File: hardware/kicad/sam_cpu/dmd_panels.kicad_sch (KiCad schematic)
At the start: 20 parts, among them J25 J25 HUB75 PANEL A, J26 J26 HUB75 PANEL B, U27 74AHCT245, U28 74AHCT245, U29 74AHCT245, U30 74HC165, U31 74HC595

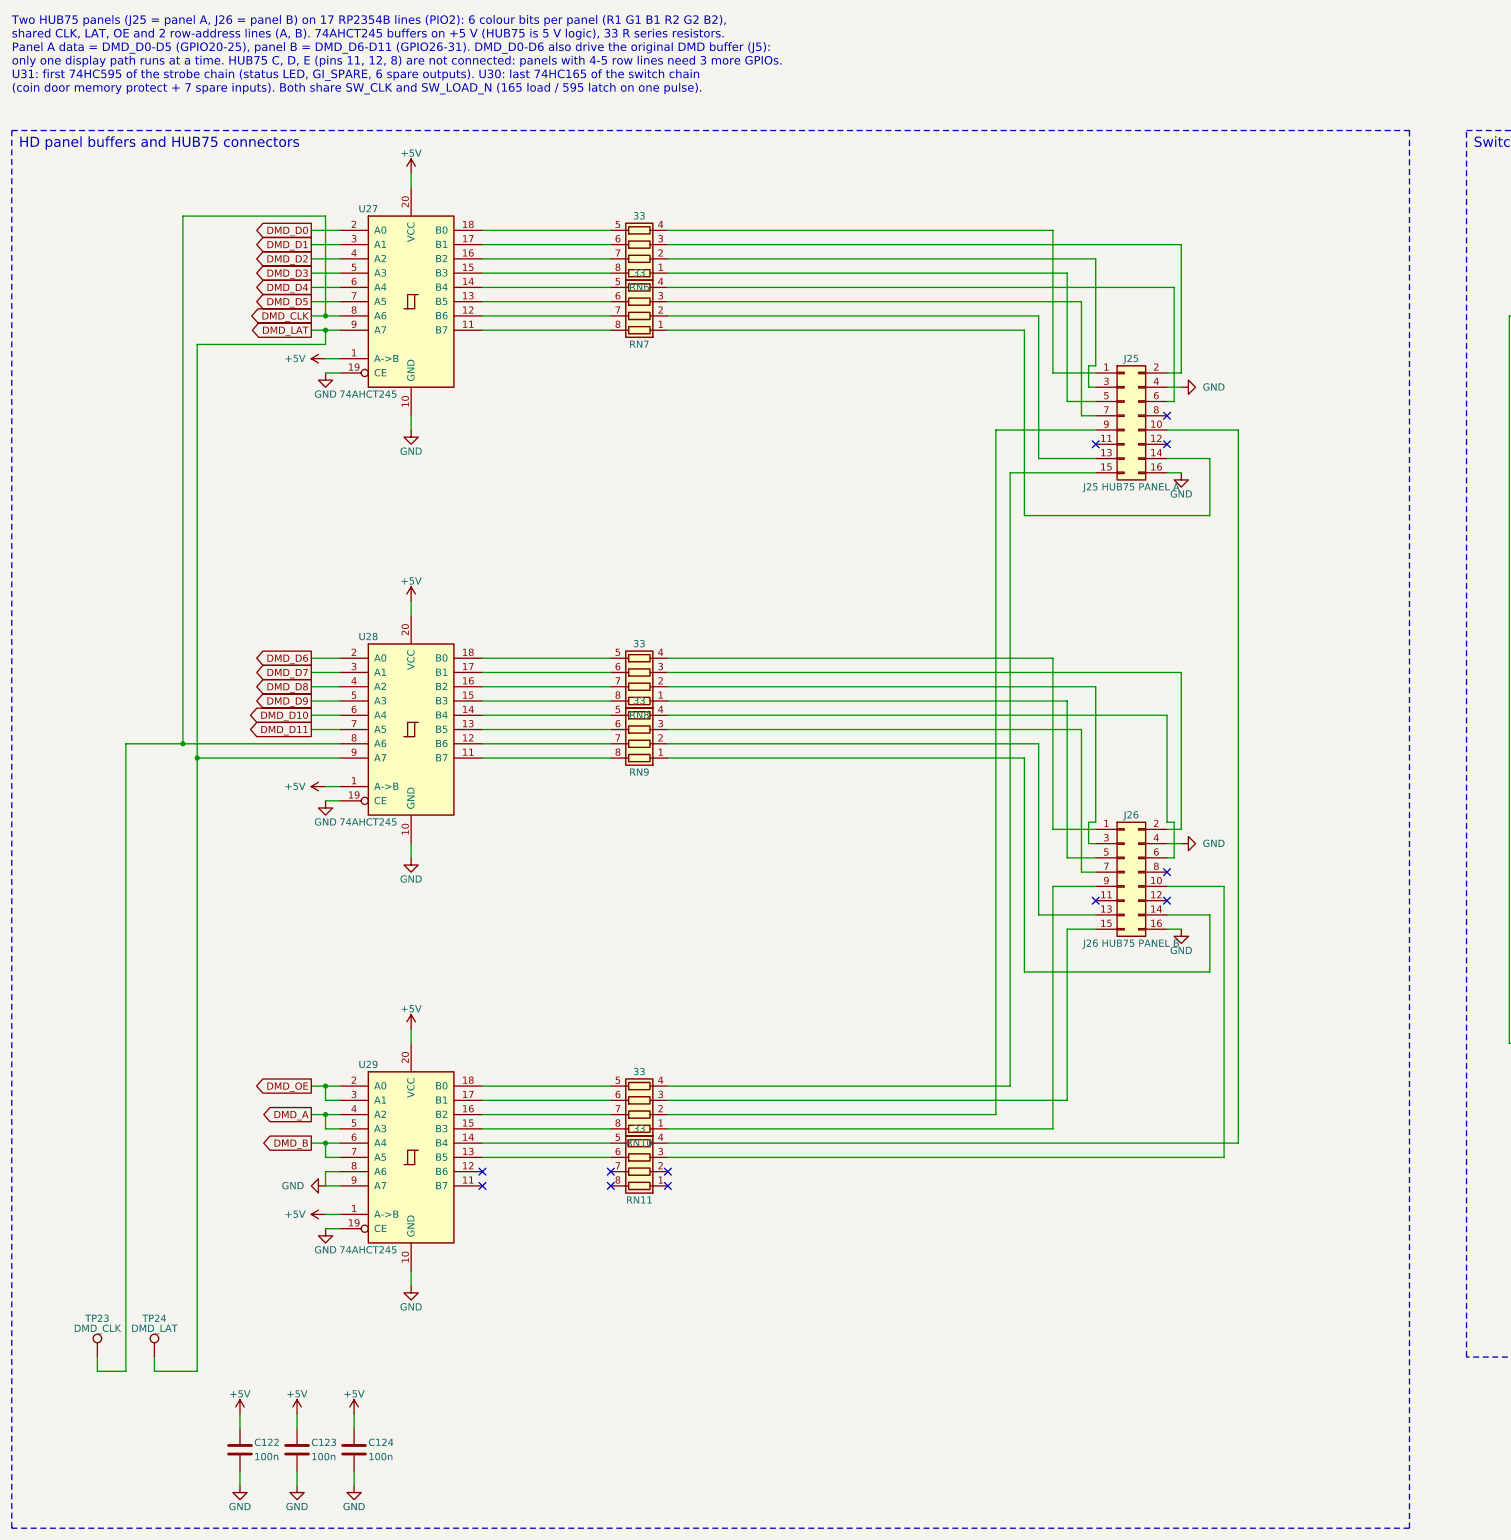
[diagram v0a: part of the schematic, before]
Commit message: Remove both DMD interfaces from the schematic and the board
DMD signals do not survive the long cabinet wires (Vincent, 2026-10-07).
Removed: J5 original DMD driver (U21, RN4, RN5, R176-R182, C95) and the
HD panel bus (J25, J26, U27-U29, RN6-RN11, C122-C124, TP23, TP24), their
tracks and fan-out vias. U30 / U31 stay (switch chain). RP2354B GPIO20-36
are unassigned (no-connect flags). The board goes back to the original
120.65 x 231.76 mm outline. DRC: 20 connections still open (was 35).

Co-Authored-By: Claude Opus 5.5 (1M context) <noreply@anthropic.com>
Claude-Session: https://claude.ai/code/session_01ExuDVoDDDHhVWjb8EwVzYb
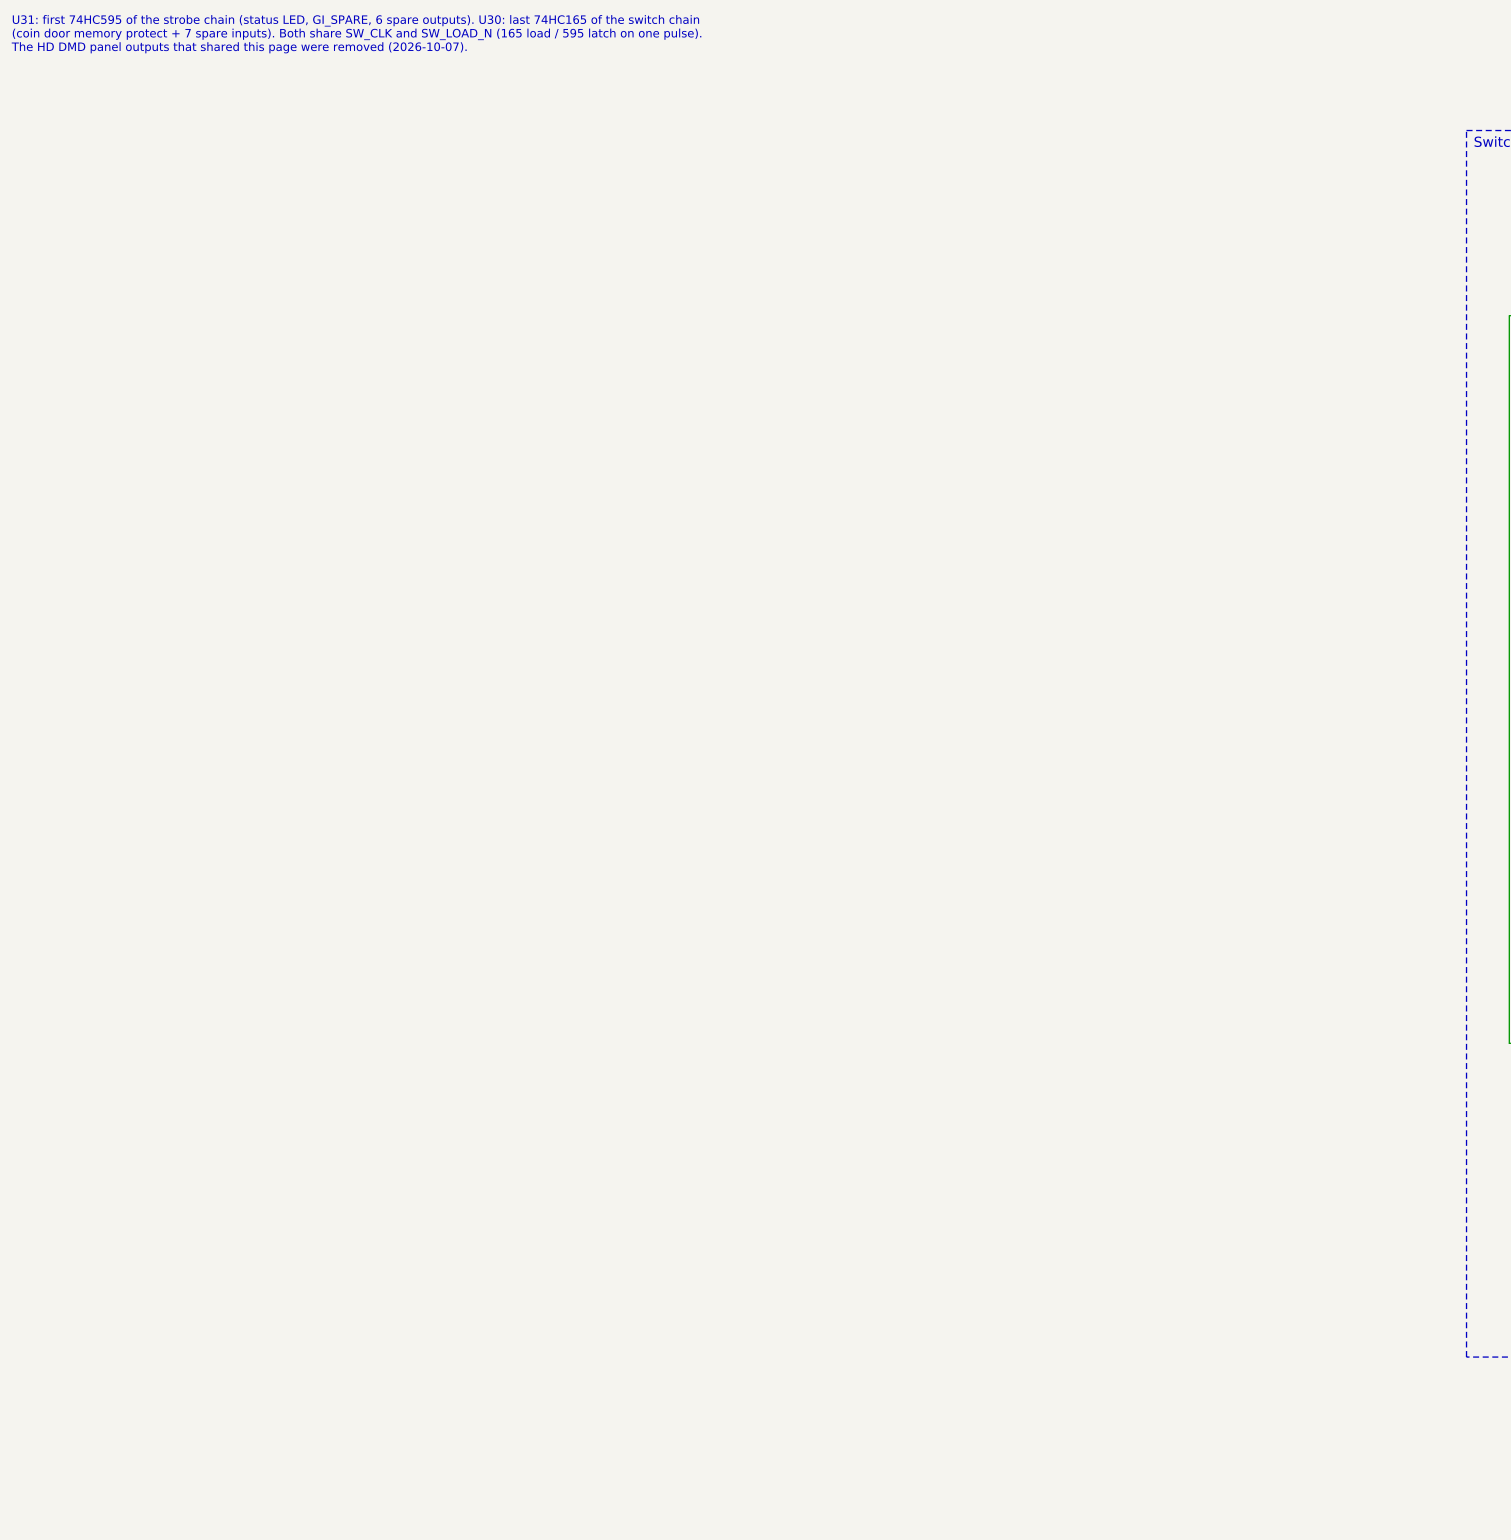
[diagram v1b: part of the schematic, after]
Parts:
- removed C122, C123, C124: 100n, Capacitor_SMD:C_0603_1608Metric, symbol Device:C
- removed J25: J25 HUB75 PANEL A, Connector_IDC:IDC-Header_2x08_P2.54mm_Vertical, symbol Connector_Generic:Conn_02x08_Odd_Even
- removed J26: J26 HUB75 PANEL B, Connector_IDC:IDC-Header_2x08_P2.54mm_Vertical, symbol Connector_Generic:Conn_02x08_Odd_Even
- removed RN10, RN11, RN6, RN7, RN8, RN9: 33, Resistor_SMD:R_Array_Convex_4x0603, symbol Device:R_Pack04
- removed TP23: DMD_CLK, TestPoint:TestPoint_Pad_D1.5mm, symbol Connector:TestPoint
- removed TP24: DMD_LAT, TestPoint:TestPoint_Pad_D1.5mm, symbol Connector:TestPoint
- removed U27, U28, U29: 74AHCT245, Package_SO:TSSOP-20_4.4x6.5mm_P0.65mm, symbol 74xx:74HC245
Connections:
- no-connect marks 19 -> 7
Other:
- note added: "U31: first 74HC595 of the strobe chain (status LED, GI_SPARE, 6 spare outputs). U30: last 74HC165 of the switch chain (coin door memory protect + 7 spare inputs). Both share SW_CLK and SW_LOAD_N (165 load / 595 latch on one pulse). The HD DMD panel outputs that shared this page were removed (2026-10-07)."
- note removed: "HD panel buffers and HUB75 connectors"
- note removed: "Two HUB75 panels (J25 = panel A, J26 = panel B) on 17 RP2354B lines (PIO2): 6 colour bits per panel (R1 G1 B1 R2 G2 B2), shared CLK, LAT, OE and 2 row-address lines (A, B). 74AHCT245 buffers on +5 V (HUB75 is 5 V logic), 33 R series resistors. Panel A data = DMD_D0-D5 (GPIO20-25), panel B = DMD_D6-D11 (GPIO26-31). DMD_D0-D6 also drive the original DMD buffer (J5): only one display path runs at a 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"

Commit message: Add an RS485 port (RJ45) and an I2S input header
Vincent, 2026-10-07: one RS485 port for both set-ups. With the Pi on J21
it is the Pi's UART3 (GPIO4 / 5, RTS on GPIO7 as driver enable); with a
remote Pi it is the RP2354B's UART1 (GPIO20 / 21, GPIO22 driver enable),
and the remote Pi's I2S reaches the DAC on J28. Both sides reach the
THVD1450 through 1 k, so only the configured side drives.

New page 13 (U32, R204-R212, C127, D27, JP2, J27, J28), RS485 labels on
the MCU sheet, and the 15 footprints placed without moving any part: the
RJ45 on the right edge where J5 was. README / PCB.md updated for draft 0.6
(DMD removal included). ERC clean; the new nets are not routed yet.

Co-Authored-By: Claude Opus 5.5 (1M context) <noreply@anthropic.com>
Claude-Session: https://claude.ai/code/session_01ExuDVoDDDHhVWjb8EwVzYb
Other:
- title: HD DMD panels (HUB75) and switch-chain extensions -> Switch-chain extensions: 7th 74HC165, first 74HC595
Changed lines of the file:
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@@
 	(paper "A3")
 	(title_block
-		(title "HD DMD panels (HUB75) and switch-chain extensions")
+		(title "Switch-chain extensions: 7th 74HC165, first 74HC595")
 		(date "2026-10-06")
 		(rev "0.2")

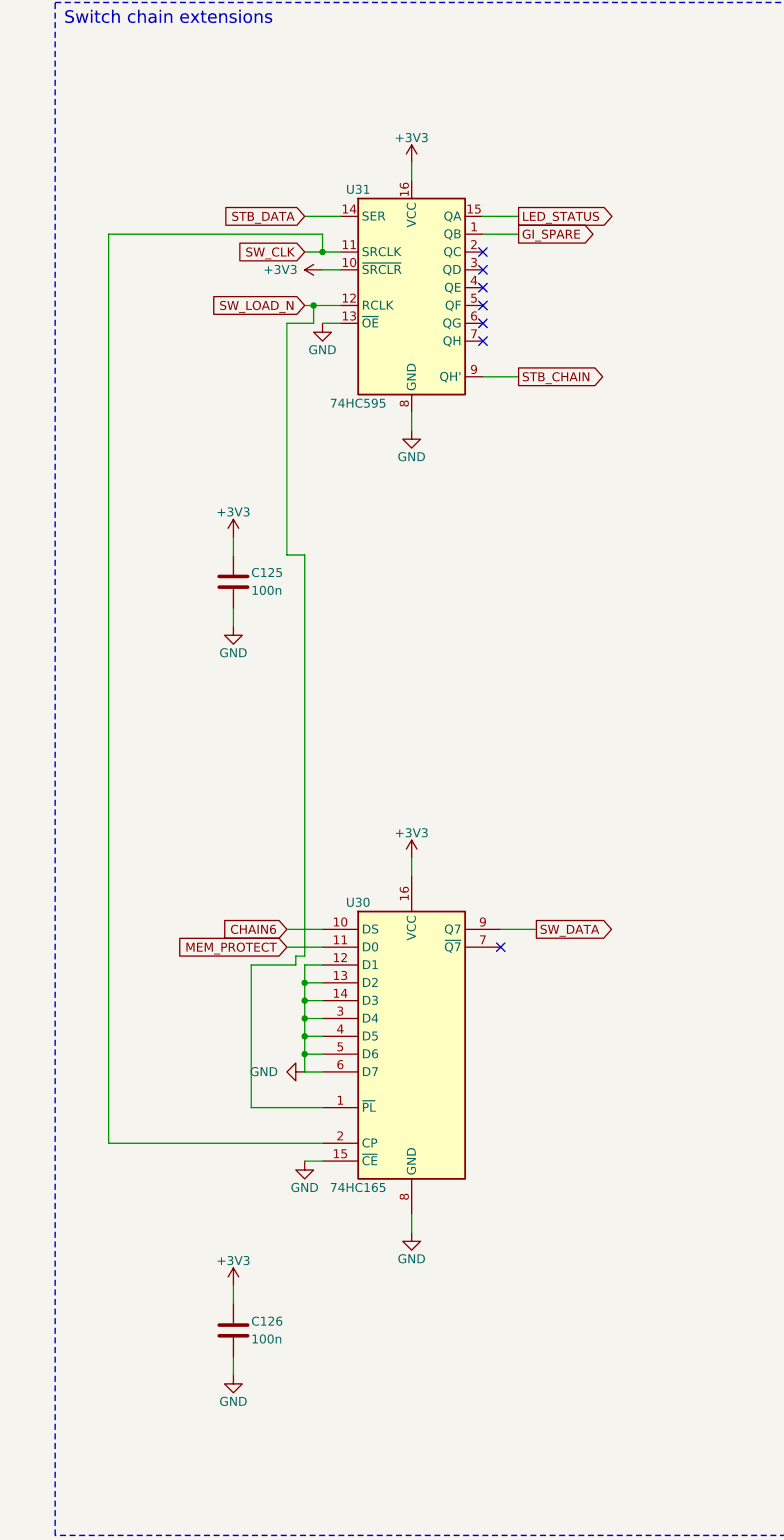
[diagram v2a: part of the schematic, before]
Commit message: DIP switch block not loaded; larger schematic text
c30: SW3, R168-R175, U14 and C93 flagged DNP (schematic and board).
c31: schematic text 1.27 -> 1.6 mm (pins 1.5 mm), intersheet refs moved out.

Co-Authored-By: Claude Opus 5.5 (1M context) <noreply@anthropic.com>
Claude-Session: https://claude.ai/code/session_01ExuDVoDDDHhVWjb8EwVzYb
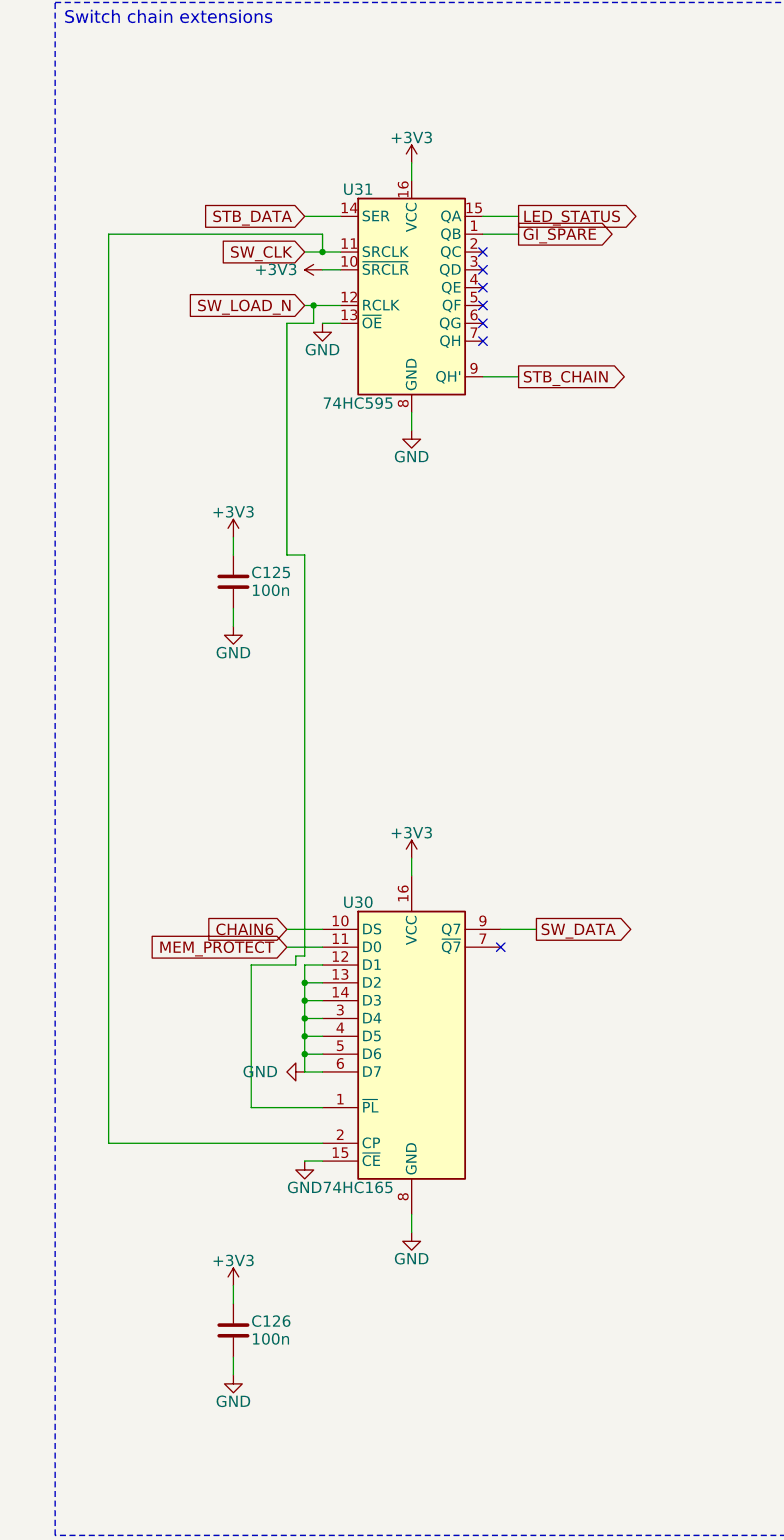
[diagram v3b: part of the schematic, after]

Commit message: Remove USB-C, GI dimmer, SWD header and DIP block; Pi SWD on GPIO24/25 as raspberrypi-swd.cfg
c35 (schematic) and c36 (board): J19 with R10-R14, the GI dimmer sheet (J18, R183-R185),
J20, and the DIP block (SW3, R168-R175, C93, U14) go to free routing space. U15's serial
input goes to GND. J21 pin 18 (GPIO24) is now SWDIO and pin 22 (GPIO25) SWCLK, matching
Raspberry Pi's OpenOCD interface/raspberrypi-swd.cfg. ERC clean, schematic parity clean.

Co-Authored-By: Claude Opus 5.5 (1M context) <noreply@anthropic.com>
Claude-Session: https://claude.ai/code/session_01QQate2kninVTv93dgZ4pfZ
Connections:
- net GI_SPARE: no longer names the net of U31.1 (QB)
- no-connect marks 7 -> 8
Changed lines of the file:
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@@
-	(wire
-		(pts
-			(xy 335.28 68.58) (xy 340.36 68.58)
-		)
-		(stroke
-			(width 0)
-			(type default)
-		)
-	)
 	(wire
 		(pts
@@
 				)
 				(justify right)
-			)
-		)
-	)
-	(global_label "GI_SPARE"
-		(shape output)
-		(at 340.36 68.58 0)
-		(fields_autoplaced yes)
-		(effects
-			(font
-				(size 1.6 1.6)
-			)
-			(justify left)
-		)
-		(property "Intersheetrefs" "${INTERSHEET_REFS}"
-			(at 357.44 68.58 0)
-			(show_name no)
-			(do_not_autoplace no)
-			(effects
-				(font
-					(size 1.6 1.6)
-				)
-				(justify left)
 			)
 		)
@@
 		)
 	)
+	(no_connect
+		(at 335.28 68.58)
+	)
 )
